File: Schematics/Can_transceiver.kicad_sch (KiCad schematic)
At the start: 6 parts, among them U8 SN65HVD230

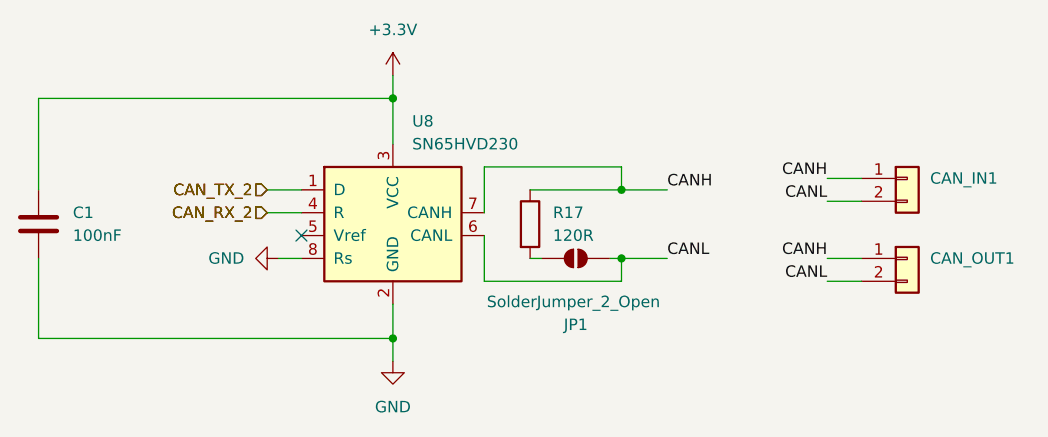
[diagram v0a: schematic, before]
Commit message: added LCSC numbers and footprint values, need to connect schemeatic pins, then can start layout
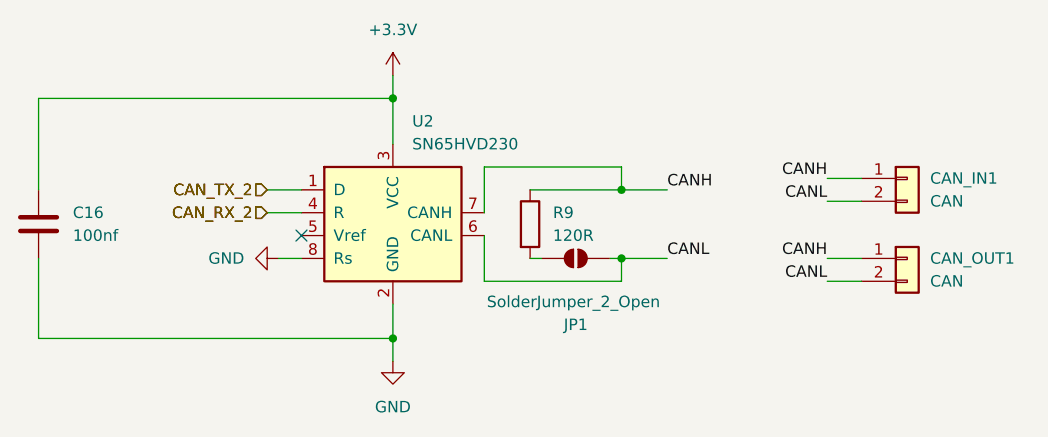
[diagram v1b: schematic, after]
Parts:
- C16: renamed from C1; value 100nF -> 100nf; footprint Capacitor_SMD:C_1210_3225Metric_Pad1.33x2.70mm_HandSolder -> Capacitor_SMD:C_0805_2012Metric_Pad1.18x1.45mm_HandSolder; LCSC Part (none) -> C49678
- CAN_IN1, CAN_OUT1: value ~ -> CAN; LCSC Part (none) -> C17644051
- R9: renamed from R17; footprint Resistor_SMD:R_0603_1608Metric -> Resistor_SMD:R_0805_2012Metric_Pad1.20x1.40mm_HandSolder; LCSC Part (none) -> C269726
- U2: renamed from U8; LCSC Part (none) -> C1543812
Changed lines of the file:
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@@
+			)
+		)
+		(property "Sim.Device" ""
+			(at 161.29 93.98 0)
+			(effects
+				(font
+					(size 1.27 1.27)
+				)
+				(hide yes)
+			)
+		)
+		(property "Sim.Type" ""
+			(at 161.29 93.98 0)
+			(effects
+				(font
+					(size 1.27 1.27)
+				)
+				(hide yes)
 			)
 		)
@@
 			)
 		)
-		(property "Value" "~"
+		(property "Value" "CAN"
 			(at 200.66 87.6299 0)
 			(effects
@@
 		)
 		(property "Description" "Generic connector, single row, 01x02, script generated (kicad-library-utils/schlib/autogen/connector/)"
+			(at 198.12 85.09 0)
+			(effects
+				(font
+					(size 1.27 1.27)
+				)
+				(hide yes)
+			)
+		)
+		(property "LCSC Part" "C17644051"
+			(at 198.12 85.09 0)
+			(effects
+				(font
+					(size 1.27 1.27)
+				)
+				(hide yes)
+			)
+		)
+		(property "Sim.Device" ""
+			(at 198.12 85.09 0)
+			(effects
+				(font
+					(size 1.27 1.27)
+				)
+				(hide yes)
+			)
+		)
+		(property "Sim.Type" ""
 			(at 198.12 85.09 0)
 			(effects
@@
 		(on_board yes)
 		(dnp no)
-		(property "Reference" "C1"
+		(property "Reference" "C16"
 			(at 105.41 88.8999 0)
 			(effects
@@
 			)
 		)
-		(property "Value" "100nF"
+		(property "Value" "100nf"
 			(at 105.41 91.4399 0)
 			(effects
@@
 			)
 		)
-		(property "Footprint" "Capacitor_SMD:C_1210_3225Metric_Pad1.33x2.70mm_HandSolder"
+		(property "Footprint" "Capacitor_SMD:C_0805_2012Metric_Pad1.18x1.45mm_HandSolder"
 			(at 102.5652 93.98 0)
 			(effects
@@
 			)
 		)
+		(property "Sim.Device" ""
+			(at 101.6 90.17 0)
+			(effects
+				(font
+					(size 1.27 1.27)
+				)
+				(hide yes)
+			)
+		)
+		(property "Sim.Type" ""
+			(at 101.6 90.17 0)
+			(effects
+				(font
+					(size 1.27 1.27)
+				)
+				(hide yes)
+			)
+		)
+		(property "LCSC Part" "C49678"
+			(at 101.6 90.17 0)
+			(effects
+				(font
+					(size 1.27 1.27)
+				)
+				(hide yes)
+			)
+		)
 		(pin "1"
 		)
@@
 			(project "flightcomputer2"
 				(path "/6cb3dda3-5fe8-4715-b831-354360aa3199/83b93a99-cc2b-4131-8387-83d6bf066ab3"
-					(reference "C1")
+					(reference "C16")
 					(unit 1)
 				)
@@
 		(dnp no)
 		(fields_autoplaced yes)
-		(property "Reference" "R17"
+		(property "Reference" "R9"
 			(at 158.75 88.8999 0)
 			(effects
@@
 			)
 		)
-		(property "Footprint" "Resistor_SMD:R_0603_1608Metric"
+		(property "Footprint" "Resistor_SMD:R_0805_2012Metric_Pad1.20x1.40mm_HandSolder"
 			(at 154.432 90.17 90)
 			(effects
@@
 			)
 		)
+		(property "Sim.Device" ""
+			(at 156.21 90.17 0)
+			(effects
+				(font
+					(size 1.27 1.27)
+				)
+				(hide yes)
+			)
+		)
+		(property "Sim.Type" ""
+			(at 156.21 90.17 0)
+			(effects
+				(font
+					(size 1.27 1.27)
+				)
+				(hide yes)
+			)
+		)
+		(property "LCSC Part" "C269726"
+			(at 156.21 90.17 0)
+			(effects
+				(font
+					(size 1.27 1.27)
+				)
+				(hide yes)
+			)
+		)
 		(pin "1"
 		)
@@
 			(project "flightcomputer2"
 				(path "/6cb3dda3-5fe8-4715-b831-354360aa3199/83b93a99-cc2b-4131-8387-83d6bf066ab3"
-					(reference "R17")
+					(reference "R9")
 					(unit 1)
 				)
@@
 		(dnp no)
 		(fields_autoplaced yes)
-		(property "Reference" "U8"
+		(property "Reference" "U2"
 			(at 143.1133 78.74 0)
 			(effects
@@
 			)
 		)
+		(property "Sim.Device" ""
+			(at 140.97 88.9 0)
+			(effects
+				(font
+					(size 1.27 1.27)
+				)
+				(hide yes)
+			)
+		)
+		(property "Sim.Type" ""
+			(at 140.97 88.9 0)
+			(effects
+				(font
+					(size 1.27 1.27)
+				)
+				(hide yes)
+			)
+		)
+		(property "LCSC Part" "C1543812"
+			(at 140.97 88.9 0)
+			(effects
+				(font
+					(size 1.27 1.27)
+				)
+				(hide yes)
+			)
+		)
 		(pin "1"
 		)
@@
 			(project "flightcomputer2"
 				(path "/6cb3dda3-5fe8-4715-b831-354360aa3199/83b93a99-cc2b-4131-8387-83d6bf066ab3"
-					(reference "U8")
+					(reference "U2")
 					(unit 1)
 				)
@@
 		(dnp no)
 		(fields_autoplaced yes)
-		(property "Reference" "#PWR068"
+		(property "Reference" "#PWR038"
 			(at 140.97 77.47 0)
 			(effects
@@
 			(project "flightcomputer2"
 				(path "/6cb3dda3-5fe8-4715-b831-354360aa3199/83b93a99-cc2b-4131-8387-83d6bf066ab3"
-					(reference "#PWR068")
+					(reference "#PWR038")
 					(unit 1)
 				)
@@
 		(dnp no)
 		(fields_autoplaced yes)
-		(property "Reference" "#PWR067"
+		(property "Reference" "#PWR037"
 			(at 121.92 93.98 0)
 			(effects
@@
 			(project "flightcomputer2"
 				(path "/6cb3dda3-5fe8-4715-b831-354360aa3199/83b93a99-cc2b-4131-8387-83d6bf066ab3"
-					(reference "#PWR067")
+					(reference "#PWR037")
 					(unit 1)
 				)
@@
 			)
 		)
-		(property "Value" "~"
+		(property "Value" "CAN"
 			(at 200.66 96.5199 0)
 			(effects
@@
 		)
 		(property "Description" "Generic connector, single row, 01x02, script generated (kicad-library-utils/schlib/autogen/connector/)"
+			(at 198.12 93.98 0)
+			(effects
+				(font
+					(size 1.27 1.27)
+				)
+				(hide yes)
+			)
+		)
+		(property "LCSC Part" "C17644051"
+			(at 198.12 93.98 0)
+			(effects
+				(font
+					(size 1.27 1.27)
+				)
+				(hide yes)
+			)
+		)
+		(property "Sim.Device" ""
+			(at 198.12 93.98 0)
+			(effects
+				(font
+					(size 1.27 1.27)
+				)
+				(hide yes)
+			)
+		)
+		(property "Sim.Type" ""
 			(at 198.12 93.98 0)
 			(effects
@@
 		(dnp no)
 		(fields_autoplaced yes)
-		(property "Reference" "#PWR069"
+		(property "Reference" "#PWR039"
 			(at 140.97 111.76 0)
 			(effects
@@
 			(project "flightcomputer2"
 				(path "/6cb3dda3-5fe8-4715-b831-354360aa3199/83b93a99-cc2b-4131-8387-83d6bf066ab3"
-					(reference "#PWR069")
-					(unit 1)
-				)
+					(reference "#PWR039")
+					(unit 1)
+				)

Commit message: started lora schematic all pcb parts should be included
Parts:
- C16: lcsc C6565120 -> (none)
- R9: lcsc C4353191 -> (none)
- U2: lcsc C12084 -> (none)
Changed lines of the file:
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@@
-			)
-		)
-		(property "Sim.Device" ""
-			(at 161.29 93.98 0)
-			(effects
-				(font
-					(size 1.27 1.27)
-				)
-				(hide yes)
-			)
-		)
-		(property "Sim.Type" ""
-			(at 161.29 93.98 0)
-			(effects
-				(font
-					(size 1.27 1.27)
-				)
-				(hide yes)
 			)
 		)
@@
 			)
 		)
-		(property "Sim.Device" ""
-			(at 198.12 85.09 0)
-			(effects
-				(font
-					(size 1.27 1.27)
-				)
-				(hide yes)
-			)
-		)
-		(property "Sim.Type" ""
-			(at 198.12 85.09 0)
-			(effects
-				(font
-					(size 1.27 1.27)
-				)
-				(hide yes)
-			)
-		)
 		(pin "1"
 		)
@@
 		)
 		(property "Description" "Unpolarized capacitor"
-			(at 101.6 90.17 0)
-			(effects
-				(font
-					(size 1.27 1.27)
-				)
-				(hide yes)
-			)
-		)
-		(property "lcsc" "C6565120"
-			(at 101.6 90.17 0)
-			(effects
-				(font
-					(size 1.27 1.27)
-				)
-				(hide yes)
-			)
-		)
-		(property "Sim.Device" ""
-			(at 101.6 90.17 0)
-			(effects
-				(font
-					(size 1.27 1.27)
-				)
-				(hide yes)
-			)
-		)
-		(property "Sim.Type" ""
 			(at 101.6 90.17 0)
 			(effects
@@
 			)
 		)
-		(property "lcsc" "C4353191"
-			(at 156.21 90.17 0)
-			(effects
-				(font
-					(size 1.27 1.27)
-				)
-				(hide yes)
-			)
-		)
-		(property "Sim.Device" ""
-			(at 156.21 90.17 0)
-			(effects
-				(font
-					(size 1.27 1.27)
-				)
-				(hide yes)
-			)
-		)
-		(property "Sim.Type" ""
-			(at 156.21 90.17 0)
-			(effects
-				(font
-					(size 1.27 1.27)
-				)
-				(hide yes)
-			)
-		)
 		(property "LCSC Part" "C269726"
 			(at 156.21 90.17 0)
@@
 			)
 		)
-		(property "lcsc" "C12084"
-			(at 140.97 88.9 0)
-			(effects
-				(font
-					(size 1.27 1.27)
-				)
-				(hide yes)
-			)
-		)
-		(property "Sim.Device" ""
-			(at 140.97 88.9 0)
-			(effects
-				(font
-					(size 1.27 1.27)
-				)
-				(hide yes)
-			)
-		)
-		(property "Sim.Type" ""
-			(at 140.97 88.9 0)
-			(effects
-				(font
-					(size 1.27 1.27)
-				)
-				(hide yes)
-			)
-		)
 		(property "LCSC Part" "C1543812"
 			(at 140.97 88.9 0)
@@
 			(at 198.12 93.98 0)
 			(effects
-				(font
-					(size 1.27 1.27)
-				)
-				(hide yes)
-			)
-		)
-		(property "Sim.Device" ""
-			(at 198.12 93.98 0)
-			(effects
-				(font
-					(size 1.27 1.27)
-				)
-				(hide yes)
-			)
-		)
-		(property "Sim.Type" ""
-			(at 198.12 93.98 0)
-			(effects

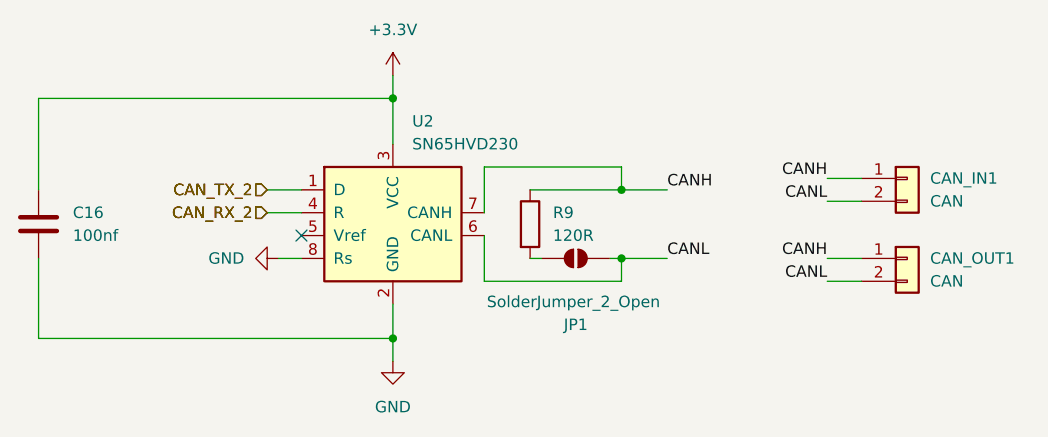
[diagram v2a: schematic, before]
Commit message: added lora correct and organizing sheet pins
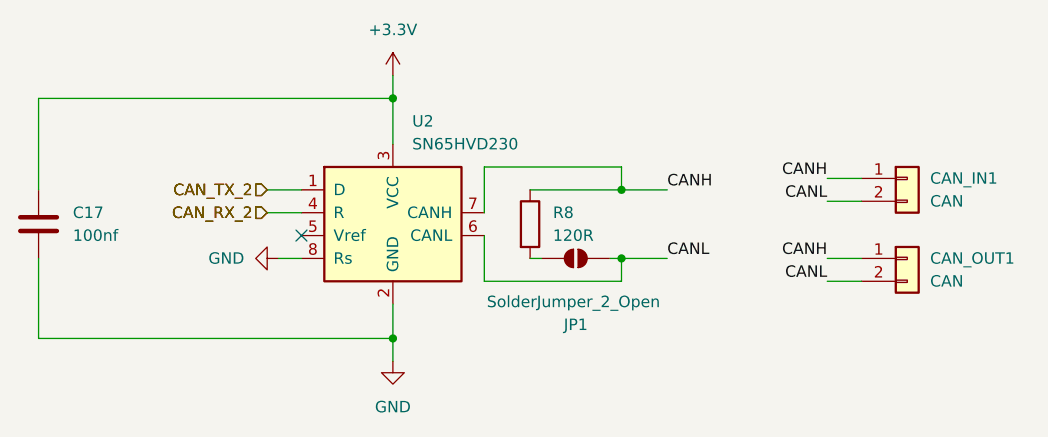
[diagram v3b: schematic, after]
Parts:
- renumbered C16 to C17, R9 to R8
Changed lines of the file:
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@@
 		(on_board yes)
 		(dnp no)
-		(property "Reference" "C16"
+		(property "Reference" "C17"
 			(at 105.41 88.8999 0)
 			(effects
@@
 			(project "flightcomputer2"
 				(path "/6cb3dda3-5fe8-4715-b831-354360aa3199/83b93a99-cc2b-4131-8387-83d6bf066ab3"
-					(reference "C16")
+					(reference "C17")
 					(unit 1)
 				)
@@
 		(dnp no)
 		(fields_autoplaced yes)
-		(property "Reference" "R9"
+		(property "Reference" "R8"
 			(at 158.75 88.8999 0)
 			(effects
@@
 			(project "flightcomputer2"
 				(path "/6cb3dda3-5fe8-4715-b831-354360aa3199/83b93a99-cc2b-4131-8387-83d6bf066ab3"
-					(reference "R9")
+					(reference "R8")
 					(unit 1)
 				)
